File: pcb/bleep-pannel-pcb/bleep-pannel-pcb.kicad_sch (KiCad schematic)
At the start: 24 parts, among them J1 CON_LED

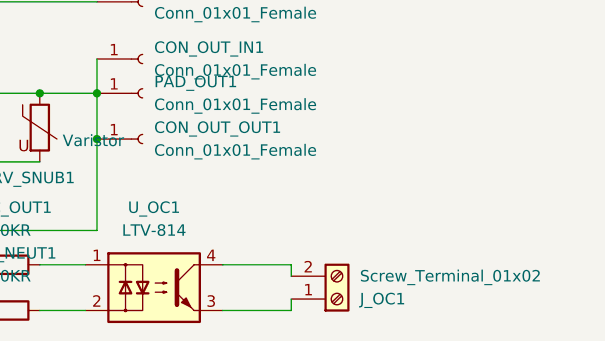
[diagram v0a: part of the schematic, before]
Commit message: Minor updates to component sizes
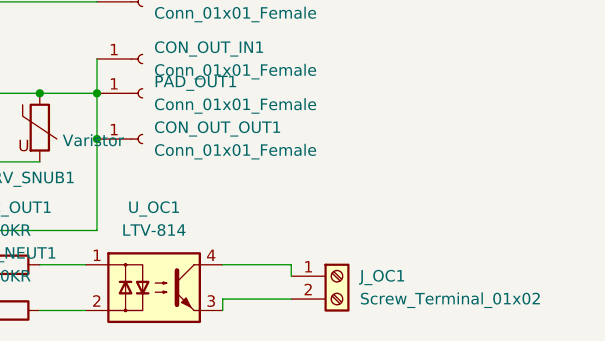
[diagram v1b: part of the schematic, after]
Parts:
- C_SNUB1: footprint Capacitor_THT:CP_Axial_L11.0mm_D5.0mm_P18.00mm_Horizontal -> Capacitor_THT:CP_Axial_L10.0mm_D6.0mm_P15.00mm_Horizontal
- RV_SNUB1: footprint Varistor:RV_Disc_D9mm_W3.3mm_P5mm -> Varistor:RV_Disc_D12mm_W3.9mm_P7.5mm
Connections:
- net at J_OC1.1 (Pin_1): now also U_OC1.4; no longer U_OC1.3
- net at J_OC1.2 (Pin_2): now also U_OC1.3; no longer U_OC1.4
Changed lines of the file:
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@@
-	(wire
-		(pts
-			(xy 203.2 138.43) (xy 210.82 138.43)
-		)
-		(stroke
-			(width 0)
-			(type default)
-		)
-	)
 	(wire
 		(pts
@@
 	(wire
 		(pts
+			(xy 189.23 96.52) (xy 189.23 91.44)
+		)
+		(stroke
+			(width 0)
+			(type default)
+		)
+	)
+	(wire
+		(pts
+			(xy 121.92 53.34) (xy 127 53.34)
+		)
+		(stroke
+			(width 0)
+			(type default)
+		)
+	)
+	(wire
+		(pts
 			(xy 210.82 133.35) (xy 210.82 134.62)
 		)
@@
 	(wire
 		(pts
-			(xy 210.82 138.43) (xy 210.82 137.16)
-		)
-		(stroke
-			(width 0)
-			(type default)
-		)
-	)
-	(wire
-		(pts
-			(xy 189.23 96.52) (xy 189.23 91.44)
-		)
-		(stroke
-			(width 0)
-			(type default)
-		)
-	)
-	(wire
-		(pts
-			(xy 121.92 53.34) (xy 127 53.34)
-		)
-		(stroke
-			(width 0)
-			(type default)
-		)
-	)
-	(wire
-		(pts
 			(xy 184.15 82.55) (xy 189.23 82.55)
 		)
@@
 	(wire
 		(pts
+			(xy 149.86 121.92) (xy 163.83 121.92)
+		)
+		(stroke
+			(width 0)
+			(type default)
+		)
+	)
+	(wire
+		(pts
+			(xy 189.23 110.49) (xy 189.23 114.3)
+		)
+		(stroke
+			(width 0)
+			(type default)
+		)
+	)
+	(wire
+		(pts
+			(xy 163.83 121.92) (xy 182.88 121.92)
+		)
+		(stroke
+			(width 0)
+			(type default)
+		)
+	)
+	(wire
+		(pts
 			(xy 203.2 133.35) (xy 210.82 133.35)
 		)
@@
 	(wire
 		(pts
-			(xy 149.86 121.92) (xy 163.83 121.92)
-		)
-		(stroke
-			(width 0)
-			(type default)
-		)
-	)
-	(wire
-		(pts
-			(xy 189.23 110.49) (xy 189.23 114.3)
-		)
-		(stroke
-			(width 0)
-			(type default)
-		)
-	)
-	(wire
-		(pts
-			(xy 163.83 121.92) (xy 182.88 121.92)
-		)
-		(stroke
-			(width 0)
-			(type default)
-		)
-	)
-	(wire
-		(pts
 			(xy 190.5 82.55) (xy 189.23 82.55)
 		)
@@
 	(wire
 		(pts
+			(xy 210.82 137.16) (xy 203.2 137.16)
+		)
+		(stroke
+			(width 0)
+			(type default)
+		)
+	)
+	(wire
+		(pts
 			(xy 190.5 72.39) (xy 190.5 77.47)
 		)
@@
 		(pts
 			(xy 189.23 129.54) (xy 175.26 129.54)
+		)
+		(stroke
+			(width 0)
+			(type default)
+		)
+	)
+	(wire
+		(pts
+			(xy 203.2 137.16) (xy 203.2 138.43)
 		)
 		(stroke
@@
 	(symbol
 		(lib_id "Connector:Screw_Terminal_01x02")
-		(at 215.9 137.16 0)
-		(mirror x)
+		(at 215.9 134.62 0)
 		(unit 1)
 		(exclude_from_sim no)
@@
 		(dnp no)
 		(property "Reference" "J_OC1"
-			(at 218.44 137.1601 0)
+			(at 218.44 134.6199 0)
 			(effects
 				(font
@@
 		)
 		(property "Value" "Screw_Terminal_01x02"
-			(at 218.44 134.6201 0)
+			(at 218.44 137.1599 0)
 			(effects
 				(font
@@
 		)
 		(property "Footprint" "TerminalBlock:TerminalBlock_Altech_AK300-2_P5.00mm"
-			(at 215.9 137.16 0)
-			(effects
-				(font
-					(size 1.27 1.27)
-				)
-				(hide yes)
-			)
-		)
-		(property "Datasheet" "~"
-			(at 215.9 137.16 0)
+			(at 215.9 134.62 0)
+			(effects
+				(font
+					(size 1.27 1.27)
+				)
+				(hide yes)
+			)
+		)
+		(property "Datasheet" "~"
+			(at 215.9 134.62 0)
 			(effects
 				(font
@@
 		)
 		(property "Description" ""
-			(at 215.9 137.16 0)
+			(at 215.9 134.62 0)
 			(effects
 				(font
@@
 			)
 		)
-		(property "Footprint" "Varistor:RV_Disc_D9mm_W3.3mm_P5mm"
+		(property "Footprint" "Varistor:RV_Disc_D12mm_W3.9mm_P7.5mm"
 			(at 181.102 118.11 90)
 			(effects
@@
 			)
 		)
-		(property "Footprint" "Capacitor_THT:CP_Axial_L11.0mm_D5.0mm_P18.00mm_Horizontal"
+		(property "Footprint" "Capacitor_THT:CP_Axial_L10.0mm_D6.0mm_P15.00mm_Horizontal"
 			(at 164.7952 121.92 0)
 			(effects

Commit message: Updates and cover
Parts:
- J1: footprint Connector_PinHeader_2.54mm:PinHeader_1x02_P2.54mm_Vertical -> Connector_PinHeader_2.54mm:PinHeader_1x02_P2.54mm_Horizontal
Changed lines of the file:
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@@
 			)
 		)
-		(property "Footprint" "Connector_PinHeader_2.54mm:PinHeader_1x02_P2.54mm_Vertical"
+		(property "Footprint" "Connector_PinHeader_2.54mm:PinHeader_1x02_P2.54mm_Horizontal"
 			(at 127 64.77 0)
 			(effects

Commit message: Change LED handling
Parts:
- removed D1: LED, LED_THT:LED_D5.0mm, symbol Device:LED
- removed J1: CON_LED, Connector_PinHeader_2.54mm:PinHeader_1x02_P2.54mm_Horizontal, symbol Connector:Conn_01x02_Female
- CON_SW1: footprint Connector_Wire:SolderWire-0.75sqmm_1x01_D1.25mm_OD3.5mm -> Connector_PinHeader_2.54mm:PinHeader_1x01_P2.54mm_Vertical
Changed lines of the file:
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@@
-	)
-	(junction
-		(at 121.92 53.34)
-		(diameter 0)
-		(color 0 0 0 0)
 	)
 	(junction
@@
 	(wire
 		(pts
-			(xy 129.54 53.34) (xy 129.54 59.69)
-		)
-		(stroke
-			(width 0)
-			(type default)
-		)
-	)
-	(wire
-		(pts
 			(xy 189.23 96.52) (xy 189.23 91.44)
 		)
@@
 	(wire
 		(pts
-			(xy 121.92 53.34) (xy 127 53.34)
-		)
-		(stroke
-			(width 0)
-			(type default)
-		)
-	)
-	(wire
-		(pts
 			(xy 210.82 133.35) (xy 210.82 134.62)
 		)
@@
 		(pts
 			(xy 88.9 53.34) (xy 91.44 53.34)
-		)
-		(stroke
-			(width 0)
-			(type default)
-		)
-	)
-	(wire
-		(pts
-			(xy 120.65 53.34) (xy 121.92 53.34)
-		)
-		(stroke
-			(width 0)
-			(type default)
-		)
-	)
-	(wire
-		(pts
-			(xy 127 53.34) (xy 127 59.69)
 		)
 		(stroke
@@
 	)
 	(symbol
-		(lib_id "Device:LED")
-		(at 125.73 53.34 0)
-		(unit 1)
-		(exclude_from_sim no)
-		(in_bom yes)
-		(on_board yes)
-		(dnp no)
-		(fields_autoplaced yes)
-		(property "Reference" "D1"
-			(at 124.1425 46.99 0)
-			(effects
-				(font
-					(size 1.27 1.27)
-				)
-			)
-		)
-		(property "Value" "LED"
-			(at 124.1425 49.53 0)
-			(effects
-				(font
-					(size 1.27 1.27)
-				)
-			)
-		)
-		(property "Footprint" "LED_THT:LED_D5.0mm"
-			(at 125.73 53.34 0)
-			(effects
-				(font
-					(size 1.27 1.27)
-				)
-				(hide yes)
-			)
-		)
-		(property "Datasheet" "~"
-			(at 125.73 53.34 0)
-			(effects
-				(font
-					(size 1.27 1.27)
-				)
-				(hide yes)
-			)
-		)
-		(property "Description" "Light emitting diode"
-			(at 125.73 53.34 0)
-			(effects
-				(font
-					(size 1.27 1.27)
-				)
-				(hide yes)
-			)
-		)
-		(pin "1"
-		)
-		(pin "2"
-		)
-		(instances
-			(project ""
-				(path "/872a4328-dfd5-4ab6-8666-3dd60418a956"
-					(reference "D1")
-					(unit 1)
-				)
-			)
-		)
-	)
-	(symbol
 		(lib_id "power:NEUT")
 		(at 81.28 67.31 0)
@@
 	)
 	(symbol
-		(lib_id "Connector:Conn_01x02_Female")
-		(at 127 64.77 90)
-		(mirror x)
-		(unit 1)
-		(exclude_from_sim no)
-		(in_bom yes)
-		(on_board yes)
-		(dnp no)
-		(property "Reference" "J1"
-			(at 125.73 62.8649 90)
-			(effects
-				(font
-					(size 1.27 1.27)
-				)
-				(justify left)
-			)
-		)
-		(property "Value" "CON_LED"
-			(at 125.73 65.4049 90)
-			(effects
-				(font
-					(size 1.27 1.27)
-				)
-				(justify left)
-			)
-		)
-		(property "Footprint" "Connector_PinHeader_2.54mm:PinHeader_1x02_P2.54mm_Horizontal"
-			(at 127 64.77 0)
-			(effects
-				(font
-					(size 1.27 1.27)
-				)
-				(hide yes)
-			)
-		)
-		(property "Datasheet" "~"
-			(at 127 64.77 0)
-			(effects
-				(font
-					(size 1.27 1.27)
-				)
-				(hide yes)
-			)
-		)
-		(property "Description" "Generic connector, single row, 01x02, script generated (kicad-library-utils/schlib/autogen/connector/)"
-			(at 127 64.77 0)
-			(effects
-				(font
-					(size 1.27 1.27)
-				)
-				(hide yes)
-			)
-		)
-		(pin "2"
-		)
-		(pin "1"
-		)
-		(instances
-			(project ""
-				(path "/872a4328-dfd5-4ab6-8666-3dd60418a956"
-					(reference "J1")
-					(unit 1)
-				)
-			)
-		)
-	)
-	(symbol
 		(lib_id "Device:Lamp")
 		(at 91.44 58.42 0)
@@
 			)
 		)
-		(property "Footprint" "Connector_Wire:SolderWire-0.75sqmm_1x01_D1.25mm_OD3.5mm"
+		(property "Footprint" "Connector_PinHeader_2.54mm:PinHeader_1x01_P2.54mm_Vertical"
 			(at 194.31 104.14 0)
 			(effects
